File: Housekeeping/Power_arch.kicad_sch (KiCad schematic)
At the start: 19 parts, among them U2 INA219AxD, U3 INA219AxD, U6 TPS562200, U7 TPS562200

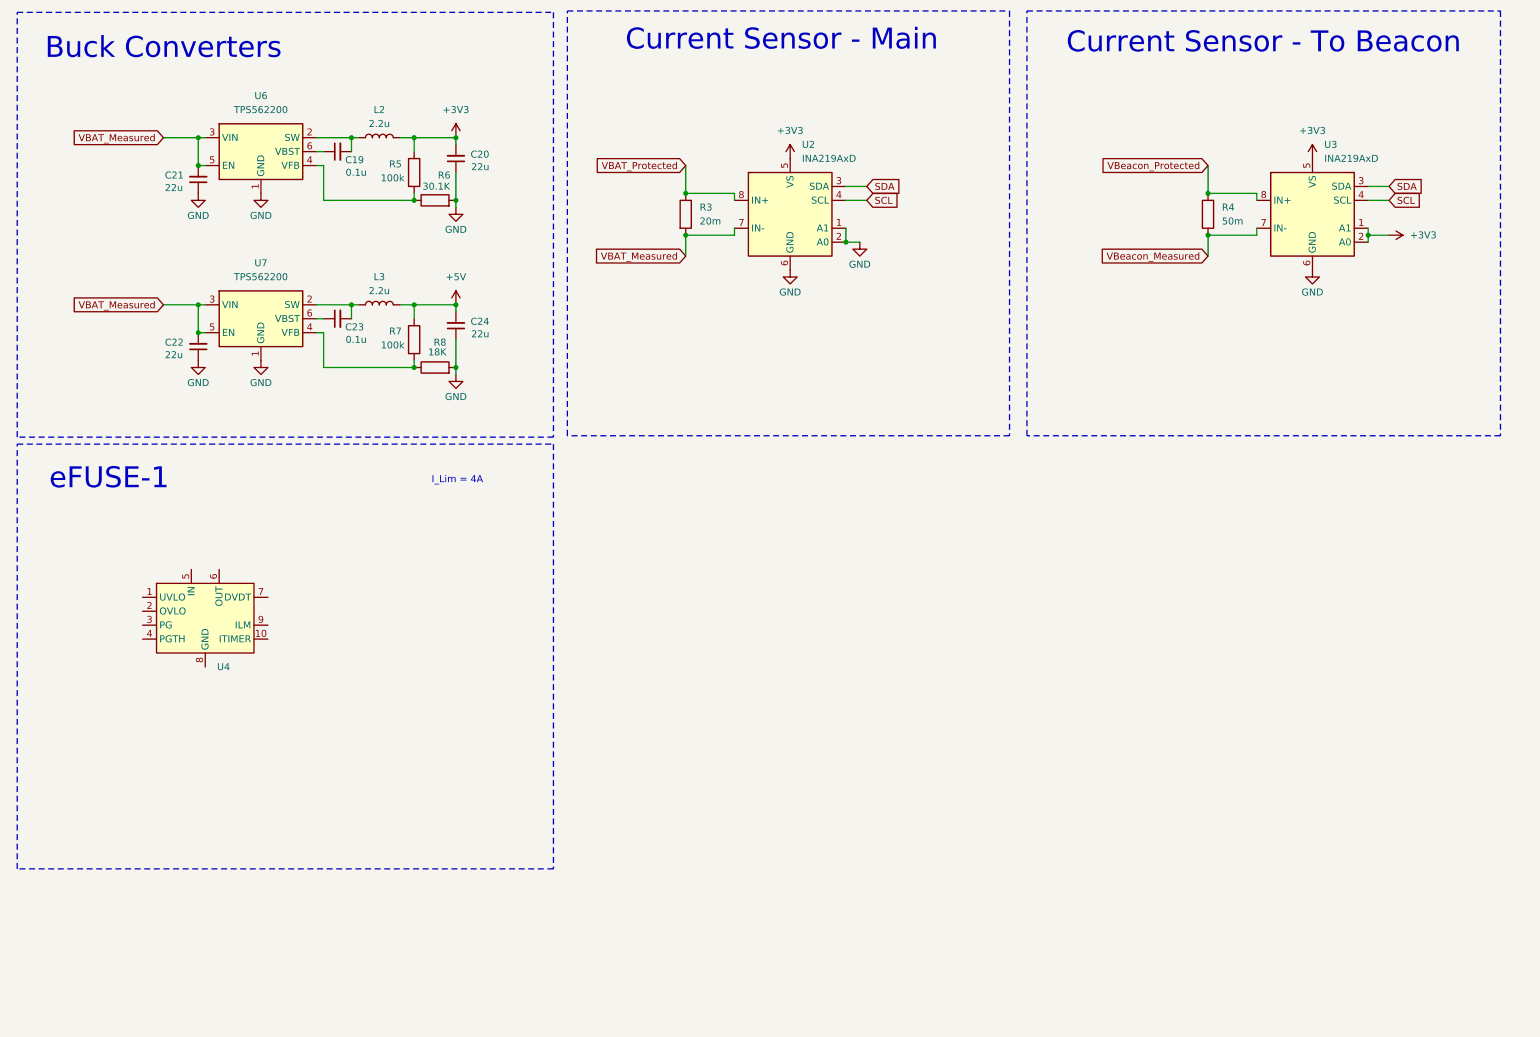
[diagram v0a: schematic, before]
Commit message: updated power arch with fuses
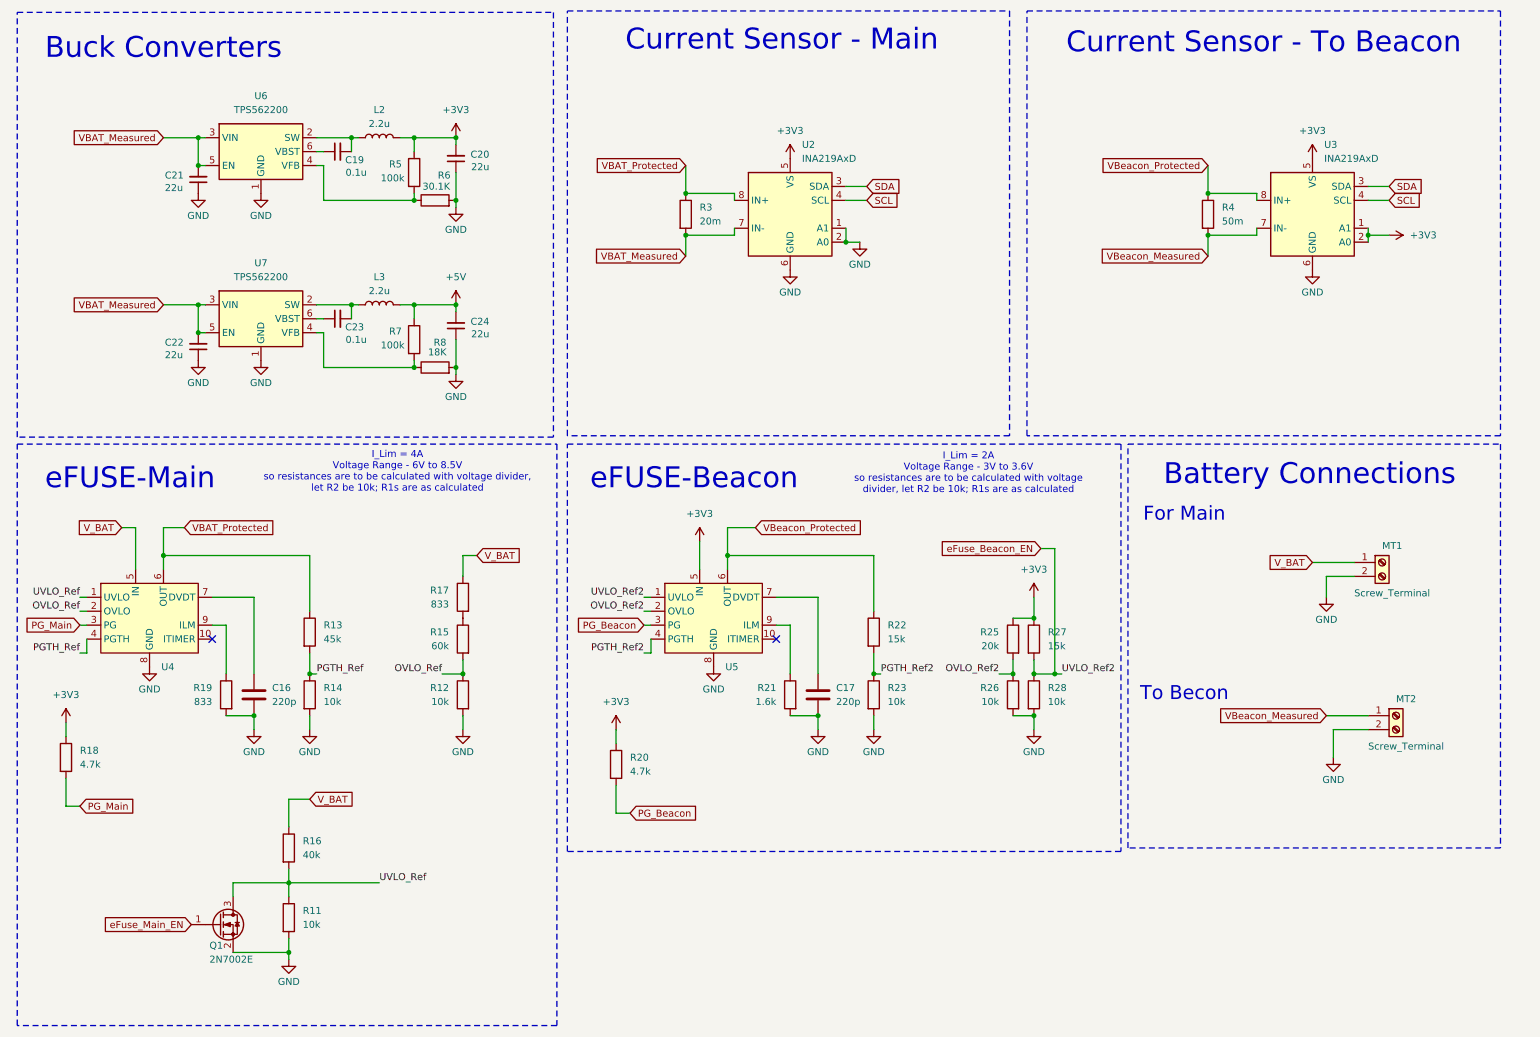
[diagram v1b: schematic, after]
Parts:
- added C16, C17: 220p, symbol Device:C
- added MT1, MT2: Screw_Terminal, TerminalBlock_Phoenix:TerminalBlock_Phoenix_MKDS-1,5-2-5.08_1x02_P5.08mm_Horizontal, symbol Connector:Screw_Terminal_01x02
- added Q1: 2N7002E, Package_TO_SOT_SMD:SOT-23, symbol Transistor_FET:2N7002E
- added R11, R12, R14, R23, R26, R28: 10k, Resistor_SMD:R_0805_2012Metric, symbol Device:R
- added R13: 45k, Resistor_SMD:R_0805_2012Metric, symbol Device:R
- added R15: 60k, Resistor_SMD:R_0805_2012Metric, symbol Device:R
- added R16: 40k, Resistor_SMD:R_0805_2012Metric, symbol Device:R
- added R17, R19: 833, Resistor_SMD:R_0805_2012Metric, symbol Device:R
- added R18, R20: 4.7k, Resistor_SMD:R_0805_2012Metric, symbol Device:R
- added R21: 1.6k, Resistor_SMD:R_0805_2012Metric, symbol Device:R
- added R22, R27: 15k, Resistor_SMD:R_0805_2012Metric, symbol Device:R
- added R25: 20k, Resistor_SMD:R_0805_2012Metric, symbol Device:R
- added U5: (no value), symbol OCPC_TPS259474L_Sybol:TPS259474L
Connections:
- net +3V3: now also R18.1, R20.1, R25.1, R27.1, U5.5 (IN)
- net GND: now also U4.8 (GND), C16.2, C17.2, MT1.2 (Pin_2), MT2.2 (Pin_2), Q1.2 (S), R11.2, R12.2, R14.2, R19.2, R21.2, R23.2, R26.2, R28.2, U5.8 (GND)
- net VBAT_Protected: now also U4.6 (OUT), R13.1
- net VBeacon_Measured: now also MT2.1 (Pin_1)
- net VBeacon_Protected: now also R22.1, U5.6 (OUT)
- net UVLO_Ref: now reaches U4.1 (UVLO)
- net UVLO_Ref: now also Q1.3 (D), R11.1, R16.2
- net OVLO_Ref: now reaches U4.2 (OVLO)
- net OVLO_Ref: now also R12.1, R15.2
- net PG_Main: now reaches U4.3 (PG)
- net PG_Main: now also R18.2
- net PGTH_Ref: now reaches U4.4 (PGTH)
- net PGTH_Ref: now also R13.2, R14.1
- net V_BAT: now reaches U4.5 (IN)
- net V_BAT: now also MT1.1 (Pin_1), R16.1, R17.1
- net at U4.7 (DVDT): now also C16.1
- net at U4.9 (ILM): now also R19.1
- new net: R21.1, U5.9 (ILM)
- new net: C17.1, U5.7 (DVDT)
- new net: R15.1, R17.2
- new net OVLO_Ref2: R25.2, R26.1, U5.2 (OVLO)
- new net PGTH_Ref2: R22.2, R23.1, U5.4 (PGTH)
- new net PG_Beacon: R20.2, U5.3 (PG)
- new net eFuse_Beacon_EN: R27.2, R28.1, U5.1 (UVLO)
- new net eFuse_Main_EN: Q1.1 (G)
- no-connect marks 0 -> 2
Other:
- note added: "Battery Connections"
- note added: "For Main To Becon"
- note added: "I_Lim = 2A Voltage Range - 3V to 3.6V so resistances are to be calculated with voltage divider, let R2 be 10k; R1s are as calculated"
- note added: "I_Lim = 4A Voltage Range - 6V to 8.5V so resistances are to be calculated with voltage divider, let R2 be 10k; R1s are as calculated"
- note added: "eFUSE-Beacon"
- note added: "eFUSE-Main"
- note removed: "I_Lim = 4A"
- note removed: "eFUSE-1"
- moved on the sheet: U4

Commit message: Implemented CAN
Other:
- note added: "3.3V Line to Beacon"
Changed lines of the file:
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@@
+		)
+	)
+	(text "3.3V Line to Beacon"
+		(exclude_from_sim no)
+		(at 250.698 138.43 0)
+		(effects
+			(font
+				(size 1.27 1.27)
+			)
 		)
 	)

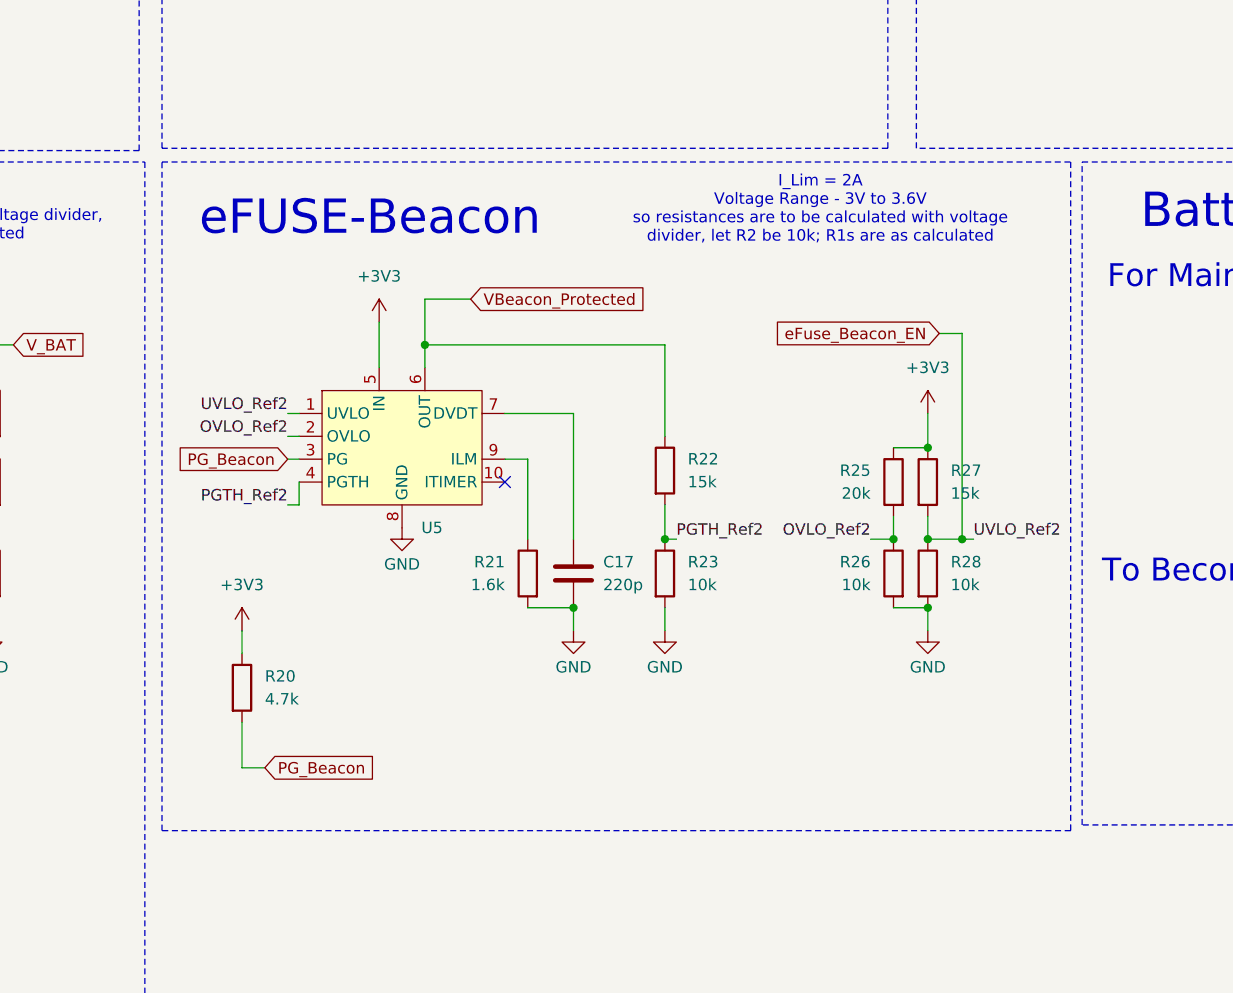
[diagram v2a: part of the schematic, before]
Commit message: added page titles to schematics
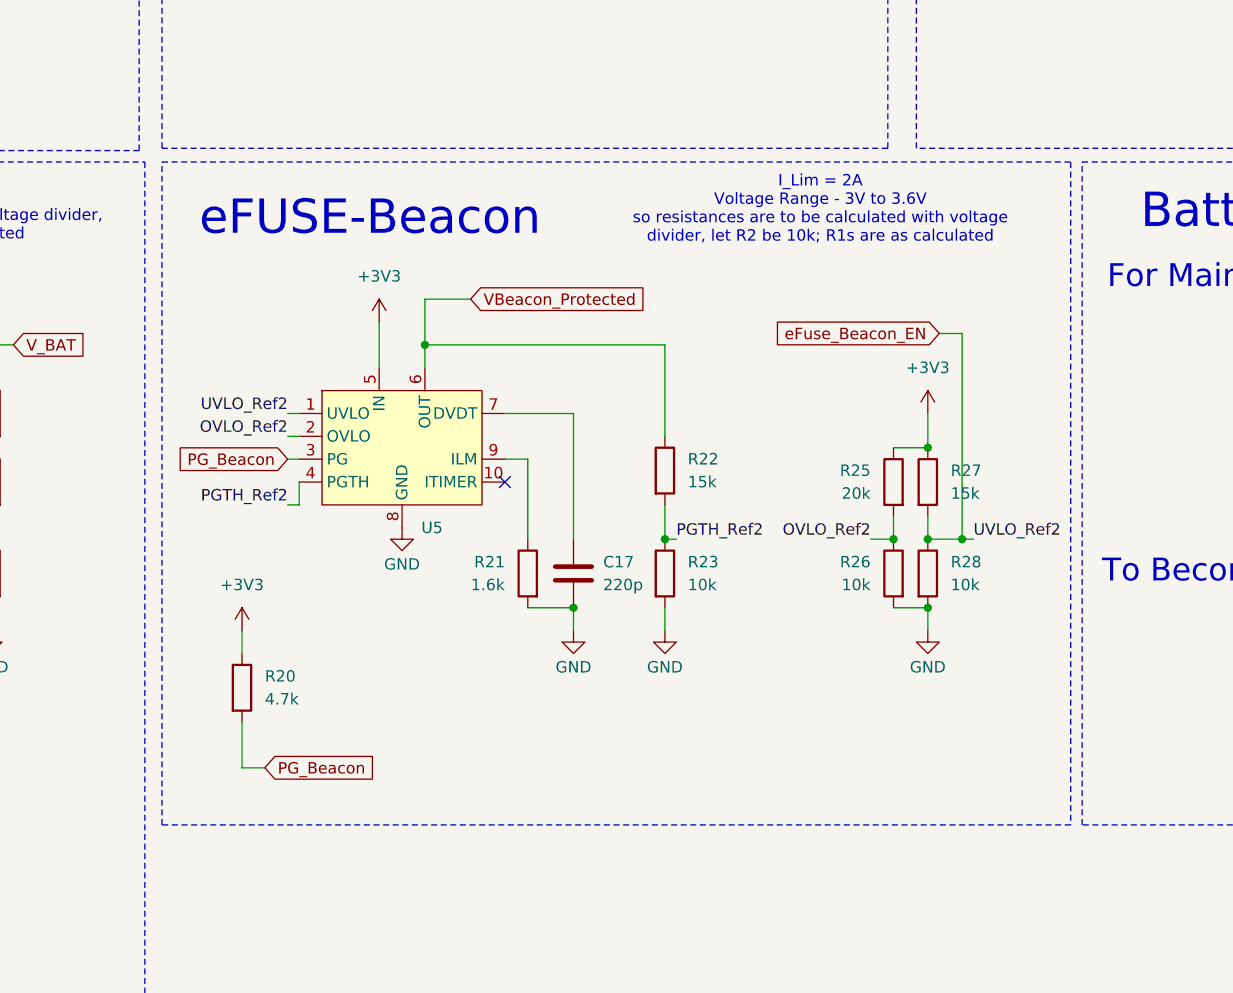
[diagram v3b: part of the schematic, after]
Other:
- company: (none) -> Team Anant - Guru Tanish
- title: (none) -> Housekeeping Board
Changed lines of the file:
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@@
 	(generator_version "10.0")
 	(paper "A4")
+	(title_block
+		(title "Housekeeping Board")
+		(company "Team Anant - Guru Tanish")
+	)
 	(rectangle
 		(start 113.03 12.446)
@@
 	(rectangle
 		(start 113.03 91.44)
-		(end 213.995 165.735)
+		(end 213.995 165.1)
 		(stroke
 			(width 0)

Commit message: Schematic V1
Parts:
- removed U5: (no value), symbol OCPC_TPS259474L_Sybol:TPS259474L
- added U10: TPS25947, Sensor_Current:Allegro_QFN-12-10-1EP_3x3mm_P0.5mm, symbol OCPC_TPS259474L_Sybol:TPS259474L
- C18: renamed from C16; footprint (none) -> Capacitor_SMD:C_0805_2012Metric
- C23: renamed from C17; footprint (none) -> Capacitor_SMD:C_0805_2012Metric
- U2: renamed from U4; value (none) -> TPS25947; footprint (none) -> Sensor_Current:Allegro_QFN-12-10-1EP_3x3mm_P0.5mm
- renumbered C21 to C16, C22 to C17, C23 to C20, C20 to C21, C24 to C22, R14 to R10, R5 to R11, R7 to R12, R6 to R13, R8 to R14, R17 to R15, R15 to R16, R12 to R17, R20 to R18, R3 to R19, R21 to R20, R22 to R21, R23 to R22, R25 to R23, R26 to R24, R27 to R25, R28 to R26, R4 to R27, R18 to R5, R19 to R6, R16 to R7, R11 to R8, R13 to R9, U6 to U3, U7 to U4, U2 to U6, U3 to U7
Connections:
- net +3V3: now also U10.1 (IN)
- net GND: now also U10.8 (GND)
- net OVLO_Ref: now also U2.6 (OVLO); no longer U2.2 (OVLO)
- net OVLO_Ref2: now also U10.6 (OVLO)
- net PGTH_Ref2: now also U10.4 (PGTH)
- net PG_Beacon: now also U10.3 (PG)
- net UVLO_Ref: now also U2.5 (UVLO); no longer U2.1 (UVLO)
- net VBAT_Protected: now also U2.2 (OUT); no longer U2.6 (OUT)
- net VBeacon_Protected: now also U10.2 (OUT)
- net V_BAT: now also U2.1 (IN); no longer U2.5 (IN)
- net eFuse_Beacon_EN: now also U10.5 (UVLO)
- net at R20.1: now also U10.9 (ILM)
- net at C23.1: now also U10.7 (DVDT)
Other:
- note added: "Voltage Range - 3V to 3.6V so resistances are to be calculated with voltage divider, let R2 be 10k; R1s are as calculated"
- note added: "Voltage Range - 6V to 8.5V so resistances are to be calculated with voltage divider, let R2 be 10k; R1s are as calculated"
- note removed: "I_Lim = 2A Voltage Range - 3V to 3.6V so resistances are to be calculated with voltage divider, let R2 be 10k; R1s are as calculated"
- note removed: "I_Lim = 4A Voltage Range - 6V to 8.5V so resistances are to be calculated with voltage divider, let R2 be 10k; R1s are as calculated"

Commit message: PCB V2
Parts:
- removed MT1, MT2: Screw_Terminal, TerminalBlock_Phoenix:TerminalBlock_Phoenix_MKDS-1,5-2-5.08_1x02_P5.08mm_Horizontal, symbol Connector:Screw_Terminal_01x02
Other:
- note removed: "3.3V Line to Beacon"
- note removed: "Battery Connections"
- note removed: "For Main To Becon"

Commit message: Added Radiation sensor and some minor changes
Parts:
- renumbered U2 to U3, U3 to U4, U4 to U5, U10 to U6, U6 to U7, U7 to U8

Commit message: Added Notes to Power Architecture for clarity
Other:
- note added: "Formulae for Tuning"
- note added: "Power Architecture Flowchart"
- note added: "R1 is between Battery and Reference R2 is between Reference and Ground"
